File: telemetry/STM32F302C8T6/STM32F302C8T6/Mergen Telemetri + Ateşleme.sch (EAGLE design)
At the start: 91 parts, among them J2 U.FL, Q2 IRLML6344TRPBF, Q3 IRLML6344TRPBF, U2 BMP280, U3 MPU-6050, U4 L86, U6 AMS1117-3.3, U7 AMS1117-3.3, U8 STM32F302C8T6, X1 JST-XH-04-PIN-LONG-PAD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

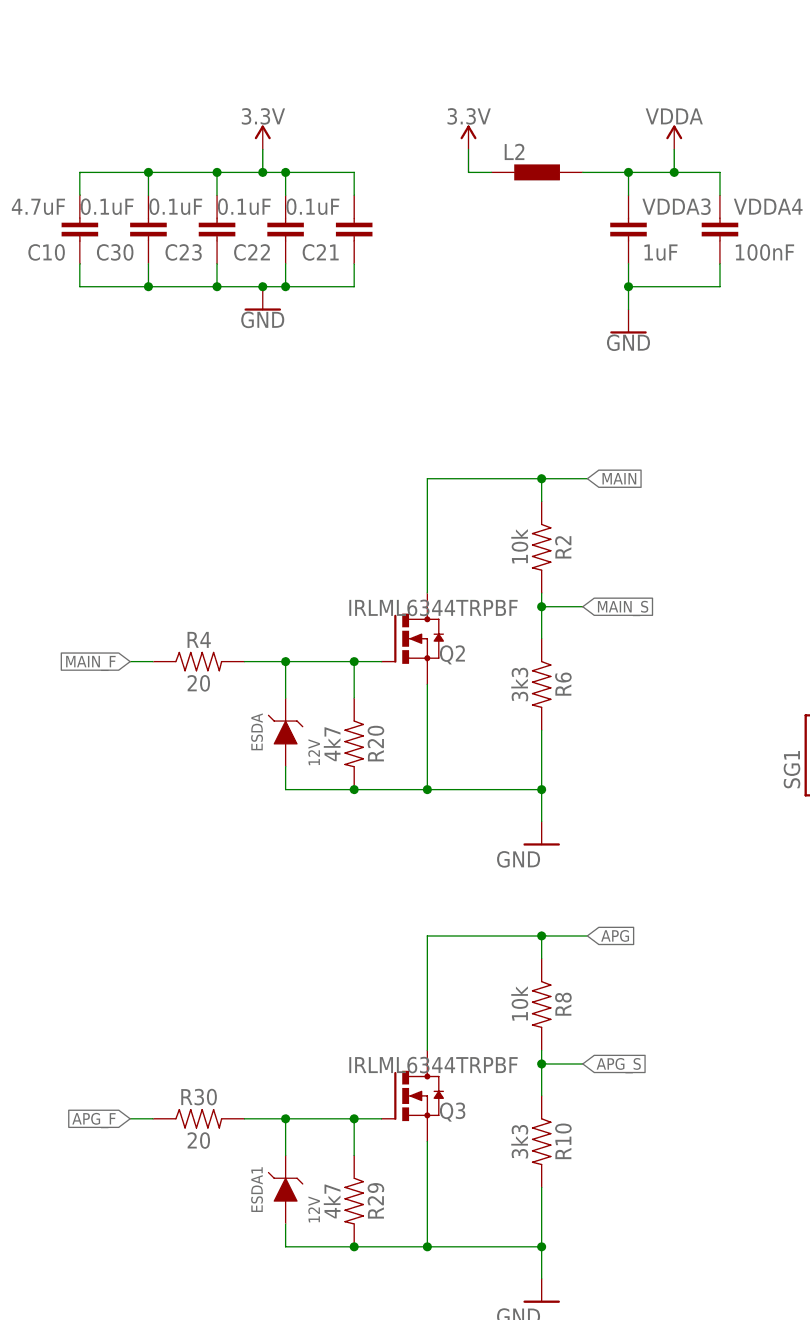
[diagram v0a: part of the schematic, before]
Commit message: packages was modified according to stock situation
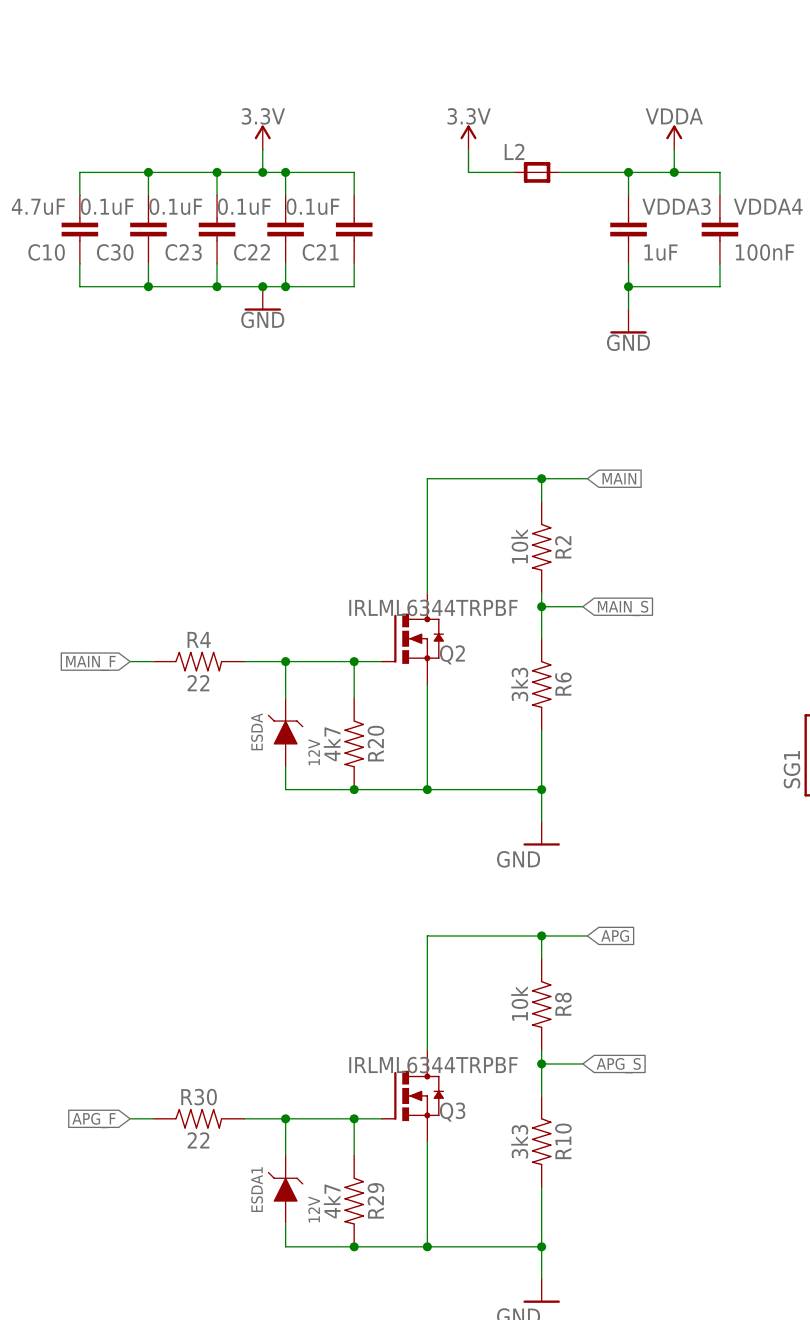
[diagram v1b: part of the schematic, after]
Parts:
- C25, C28: device SparkFun-Capacitors:47UF-POLAR-EIA3528-10V-10% -> SparkFun-Capacitors:10UF-POLAR-EIA3216-16V-10%(TANT)
- L2: value BLM15HB221SN1 -> (none); device inductors:BLM15HB221SN1 -> 52101-101-REV-A_v16:RC-MASTER-SMD_FB_0805MP
- R30, R4: value 20 -> 22
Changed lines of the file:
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@@
 <part name="VDDA4" library="SparkFun-Capacitors" library_urn="urn:adsk.eagle:library:510" deviceset="0.1UF" device="-0603-25V-(+80/-20%)" package3d_urn="urn:adsk.eagle:package:37414/1" value="100nF"/>
 <part name="GND18" library="SparkFun-PowerSymbols" library_urn="urn:adsk.eagle:library:530" deviceset="GND" device=""/>
-<part name="L2" library="inductors" library_urn="urn:adsk.eagle:library:243" deviceset="BLM15H" device="" package3d_urn="urn:adsk.eagle:package:15132/1" technology="B221SN1"/>
+<part name="L2" library="52101-101-REV-A_v16" library_urn="urn:adsk.eagle:library:21899384" deviceset="RC-MASTER-SMD_FB_" device="0805MP" package3d_urn="urn:adsk.eagle:package:15662270/2"/>
 <part name="SUPPLY20" library="SparkFun-PowerSymbols" library_urn="urn:adsk.eagle:library:530" deviceset="3.3V" device=""/>
 <part name="U$4" library="SparkFun-PowerSymbols" library_urn="urn:adsk.eagle:library:530" deviceset="VDDA" device=""/>
@@
 <part name="C31" library="SparkFun-Capacitors" library_urn="urn:adsk.eagle:library:510" deviceset="1.0UF" device="-0603-16V-10%" package3d_urn="urn:adsk.eagle:package:37414/1" value="0.1uF"/>
 <part name="C32" library="SparkFun-Capacitors" library_urn="urn:adsk.eagle:library:510" deviceset="1.0UF" device="-0603-16V-10%" package3d_urn="urn:adsk.eagle:package:37414/1" value="0.1uF"/>
-<part name="C25" library="SparkFun-Capacitors" library_urn="urn:adsk.eagle:library:510" deviceset="47UF-POLAR" device="-EIA3528-10V-10%" package3d_urn="urn:adsk.eagle:package:37411/1" value="4.7uF"/>
-<part name="C28" library="SparkFun-Capacitors" library_urn="urn:adsk.eagle:library:510" deviceset="47UF-POLAR" device="-EIA3528-10V-10%" package3d_urn="urn:adsk.eagle:package:37411/1" value="10uF"/>
+<part name="C25" library="SparkFun-Capacitors" library_urn="urn:adsk.eagle:library:27162641" deviceset="10UF-POLAR" device="-EIA3216-16V-10%(TANT)" package3d_urn="urn:adsk.eagle:package:37418/1" value="4.7uF"/>
+<part name="C28" library="SparkFun-Capacitors" library_urn="urn:adsk.eagle:library:27162641" deviceset="10UF-POLAR" device="-EIA3216-16V-10%(TANT)" package3d_urn="urn:adsk.eagle:package:37418/1" value="10uF"/>
 <part name="C5" library="SparkFun-Capacitors" library_urn="urn:adsk.eagle:library:510" deviceset="1.0UF" device="-0603-16V-10%" package3d_urn="urn:adsk.eagle:package:37414/1" value="100nF"/>
 <part name="C27" library="SparkFun-Capacitors" library_urn="urn:adsk.eagle:library:510" deviceset="1.0UF" device="-0603-16V-10%" package3d_urn="urn:adsk.eagle:package:37414/1" value="100nF"/>
@@
 <part name="R6" library="SparkFun-Resistors" library_urn="urn:adsk.eagle:library:532" deviceset="1KOHM" device="-0603-1/10W-1%" package3d_urn="urn:adsk.eagle:package:39650/1" value="3k3"/>
 <part name="R20" library="SparkFun-Resistors" library_urn="urn:adsk.eagle:library:532" deviceset="1KOHM" device="-0603-1/10W-1%" package3d_urn="urn:adsk.eagle:package:39650/1" value="4k7"/>
-<part name="R4" library="SparkFun-Resistors" library_urn="urn:adsk.eagle:library:532" deviceset="1KOHM" device="-0603-1/10W-1%" package3d_urn="urn:adsk.eagle:package:39650/1" value="20"/>
+<part name="R4" library="SparkFun-Resistors" library_urn="urn:adsk.eagle:library:532" deviceset="1KOHM" device="-0603-1/10W-1%" package3d_urn="urn:adsk.eagle:package:39650/1" value="22"/>
 <part name="R7" library="SparkFun-Resistors" library_urn="urn:adsk.eagle:library:532" deviceset="1KOHM" device="-0603-1/10W-1%" package3d_urn="urn:adsk.eagle:package:39650/1" value="220"/>
 <part name="R8" library="SparkFun-Resistors" library_urn="urn:adsk.eagle:library:532" deviceset="1KOHM" device="-0603-1/10W-1%" package3d_urn="urn:adsk.eagle:package:39650/1" value="10k"/>
 <part name="R10" library="SparkFun-Resistors" library_urn="urn:adsk.eagle:library:532" deviceset="1KOHM" device="-0603-1/10W-1%" package3d_urn="urn:adsk.eagle:package:39650/1" value="3k3"/>
 <part name="R29" library="SparkFun-Resistors" library_urn="urn:adsk.eagle:library:532" deviceset="1KOHM" device="-0603-1/10W-1%" package3d_urn="urn:adsk.eagle:package:39650/1" value="4k7"/>
-<part name="R30" library="SparkFun-Resistors" library_urn="urn:adsk.eagle:library:532" deviceset="1KOHM" device="-0603-1/10W-1%" package3d_urn="urn:adsk.eagle:package:39650/1" value="20"/>
+<part name="R30" library="SparkFun-Resistors" library_urn="urn:adsk.eagle:library:532" deviceset="1KOHM" device="-0603-1/10W-1%" package3d_urn="urn:adsk.eagle:package:39650/1" value="22"/>
 <part name="R11" library="SparkFun-Resistors" library_urn="urn:adsk.eagle:library:532" deviceset="1KOHM" device="-0603-1/10W-1%" package3d_urn="urn:adsk.eagle:package:39650/1" value="10k"/>
 <part name="SUPPLY21" library="SparkFun-PowerSymbols" library_urn="urn:adsk.eagle:library:530" deviceset="3.3V" device=""/>
@@
 <wire x1="144.78" y1="78.74" x2="144.78" y2="76.2" width="0.1524" layer="91"/>
 <pinref part="L2" gate="G$1" pin="1"/>
-<wire x1="144.78" y1="76.2" x2="147.32" y2="76.2" width="0.1524" layer="91"/>
+<wire x1="144.78" y1="76.2" x2="149.86" y2="76.2" width="0.1524" layer="91"/>
 </segment>
 <segment>
@@
 <pinref part="L2" gate="G$1" pin="2"/>
 <pinref part="VDDA4" gate="G$1" pin="1"/>
-<wire x1="157.48" y1="76.2" x2="162.56" y2="76.2" width="0.1524" layer="91"/>
+<wire x1="154.94" y1="76.2" x2="162.56" y2="76.2" width="0.1524" layer="91"/>
 <wire x1="162.56" y1="76.2" x2="167.64" y2="76.2" width="0.1524" layer="91"/>
 <wire x1="167.64" y1="76.2" x2="172.72" y2="76.2" width="0.1524" layer="91"/>
